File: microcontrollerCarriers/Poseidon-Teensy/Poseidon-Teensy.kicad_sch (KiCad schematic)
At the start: 46 parts, among them J1 Conn_01x03, J10 Conn_01x03, J11 Conn_01x03, J12 Conn_01x03, J13 Conn_01x03, J14 Conn_01x03, J15 Conn_01x03, J16 Conn_01x04, J19 Conn_01x02, J2 Conn_01x03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

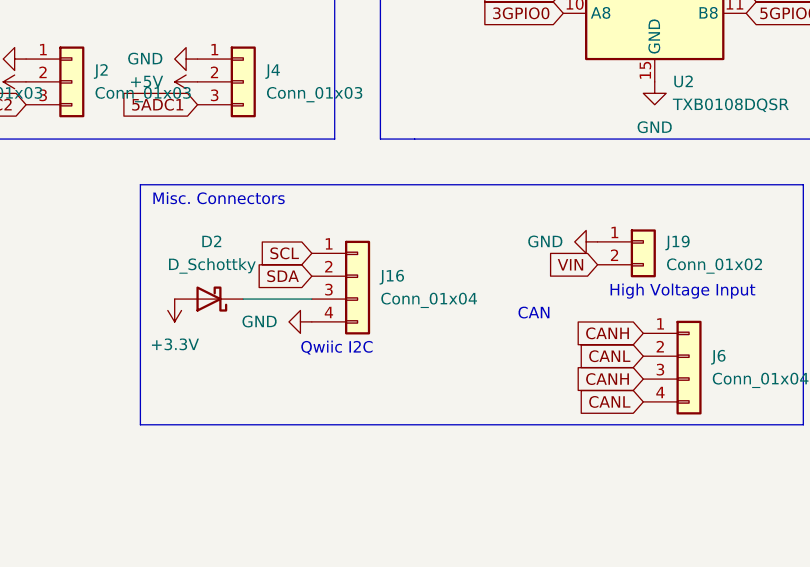
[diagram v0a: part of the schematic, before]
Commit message: Fix JST-SH 3d model and pins, add silkscreen to Pico
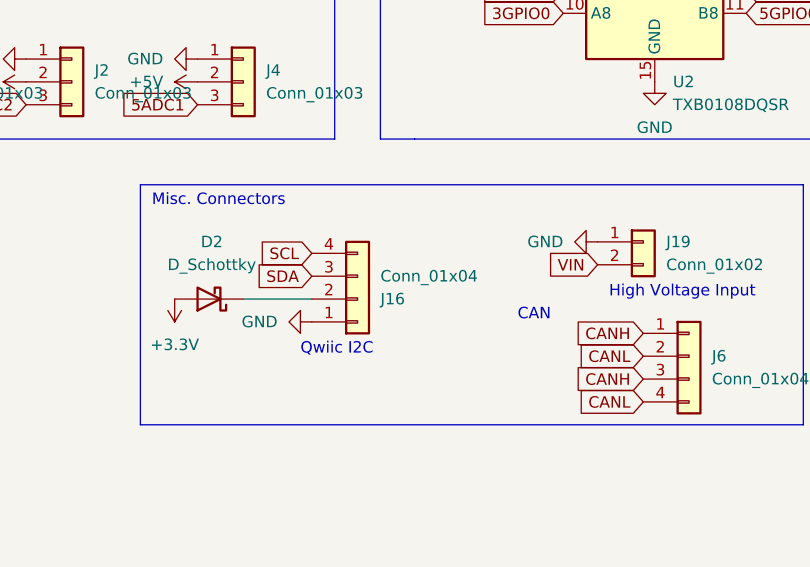
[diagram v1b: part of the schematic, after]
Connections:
- net GND: now also J16.1 (Pin_1); no longer J16.4 (Pin_4)
- net SCL: now also J16.4 (Pin_4); no longer J16.1 (Pin_1)
- net SDA: now also J16.3 (Pin_3); no longer J16.2 (Pin_2)
- net at D2.1 (K): now also J16.2 (Pin_2); no longer J16.3 (Pin_3)
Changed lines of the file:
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@@
     )
   )
-  (symbol (lib_id "Connector_Generic:Conn_01x04") (at 223.52 146.05 0) (unit 1)
-    (in_bom yes) (on_board yes) (dnp no) (fields_autoplaced)
-    (property "Reference" "J16" (at 226.06 146.0499 0)
+  (symbol (lib_id "Connector_Generic:Conn_01x04") (at 223.52 148.59 0) (mirror x) (unit 1)
+    (in_bom yes) (on_board yes) (dnp no)
+    (property "Reference" "J16" (at 226.06 148.5901 0)
       (effects (font (size 1.27 1.27)) (justify left))
     )
-    (property "Value" "Conn_01x04" (at 226.06 148.5899 0)
+    (property "Value" "Conn_01x04" (at 226.06 146.0501 0)
       (effects (font (size 1.27 1.27)) (justify left))
     )
-    (property "Footprint" "Connector_JST:JST_SH_BM04B-SRSS-TB_1x04-1MP_P1.00mm_Vertical" (at 223.52 146.05 0)
+    (property "Footprint" "Connector_JST:JST_SH_BM04B-SRSS-TB_1x04-1MP_P1.00mm_Vertical" (at 223.52 148.59 0)
       (effects (font (size 1.27 1.27)) hide)
     )
-    (property "Datasheet" "~" (at 223.52 146.05 0)
+    (property "Datasheet" "~" (at 223.52 148.59 0)
       (effects (font (size 1.27 1.27)) hide)
     )
